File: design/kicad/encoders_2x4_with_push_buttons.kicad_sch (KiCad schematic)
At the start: 0 parts

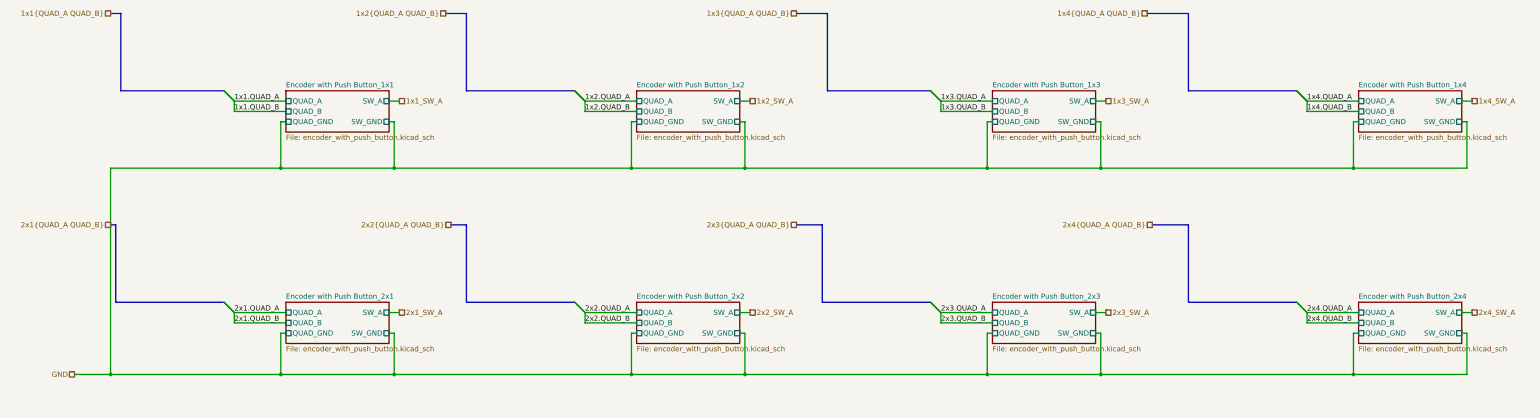
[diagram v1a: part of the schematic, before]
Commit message: Fix hardware pin configuration and rotary encoder parameters
- Updated CS_PIN from 30 to 28 in SystemConstants.hpp to reflect the correct hardware setup for ILI9341.
- Modified rotary encoder parameters in ConfigurationFactory.cpp, changing the first parameter of asRotaryEncoder from 28 to 23 for proper functionality.
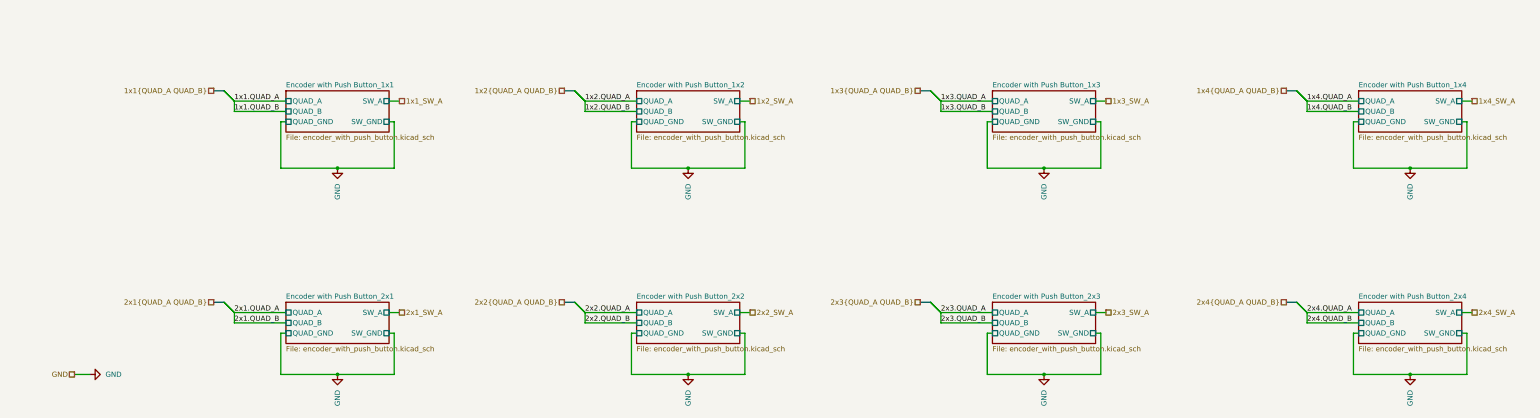
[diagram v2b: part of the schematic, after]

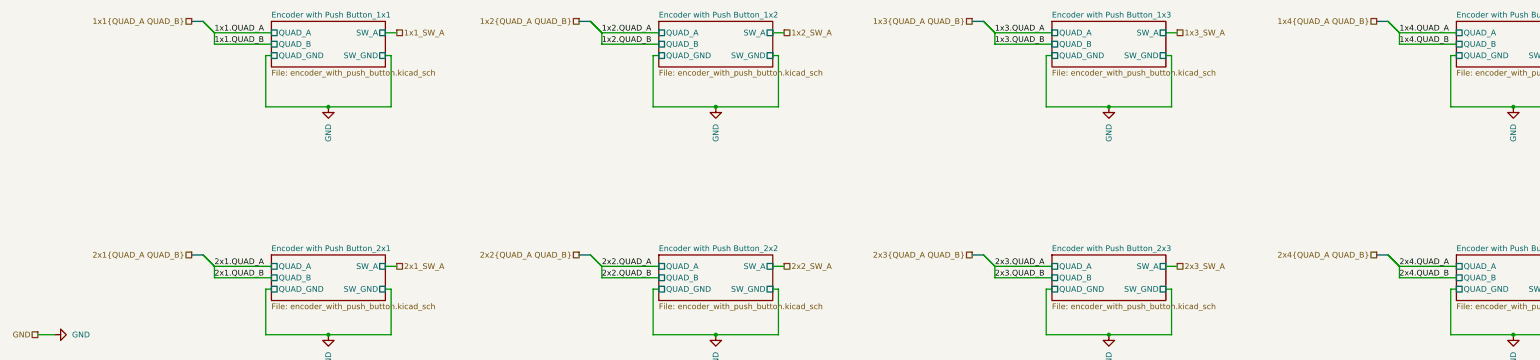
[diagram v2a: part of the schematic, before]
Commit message: Update kicad binary files
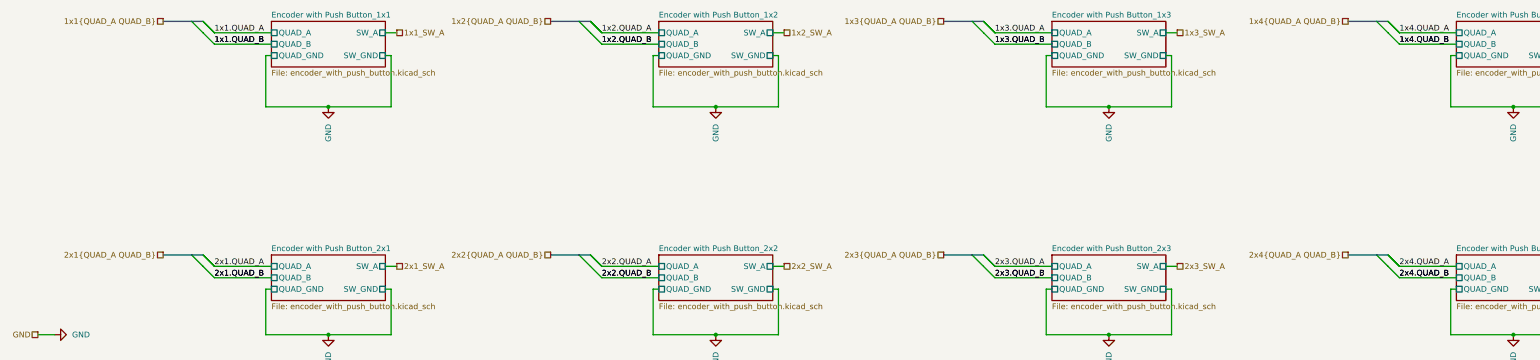
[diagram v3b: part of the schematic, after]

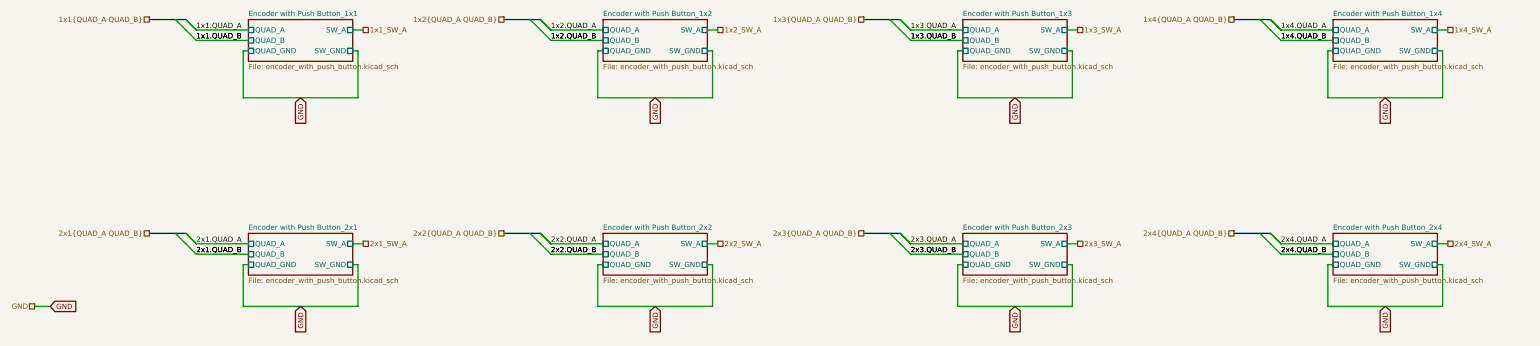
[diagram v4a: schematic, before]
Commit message: Add schematic for MIDI Display MSP2807 with associated components
- Created a new schematic file for the MIDI Display MSP2807.
- Included a unpolarized capacitor (C2) with a value of 100nF.
- Added properties such as reference, value, footprint, and datasheet for the capacitor.
- Integrated the MIDI Display module with detailed pin configurations and properties.
- Defined hierarchical labels for power and data connections (VCC, GND, CS, RST, DC, etc.).
- Ensured all components are marked for BOM inclusion and simulation.
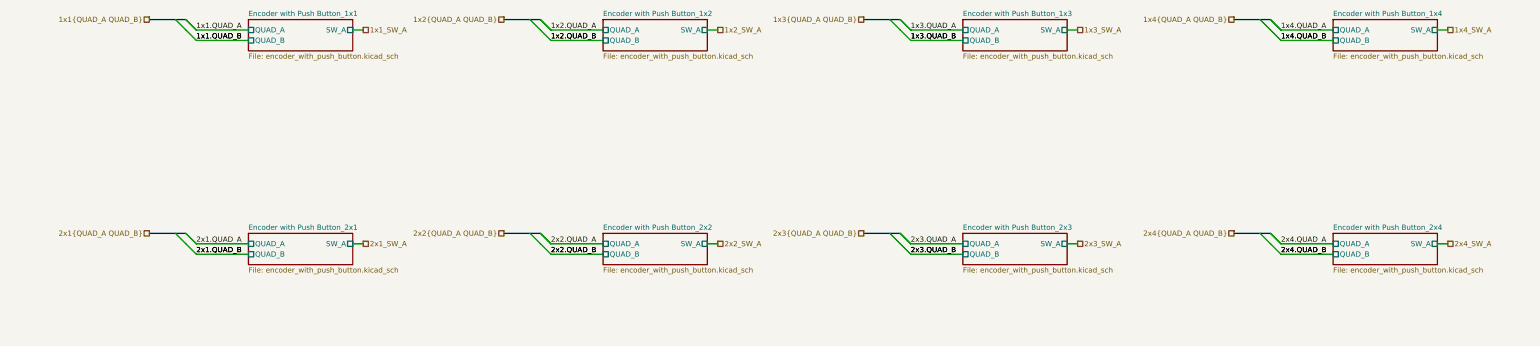
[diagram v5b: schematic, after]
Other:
- sheet Encoder with Push Button_1x1 ports: added none; removed QUAD_GND, SW_GND
- sheet Encoder with Push Button_1x2 ports: added none; removed QUAD_GND, SW_GND
- sheet Encoder with Push Button_1x3 ports: added none; removed QUAD_GND, SW_GND
- sheet Encoder with Push Button_1x4 ports: added none; removed QUAD_GND, SW_GND
- sheet Encoder with Push Button_2x1 ports: added none; removed QUAD_GND, SW_GND
- sheet Encoder with Push Button_2x2 ports: added none; removed QUAD_GND, SW_GND
- sheet Encoder with Push Button_2x3 ports: added none; removed QUAD_GND, SW_GND
- sheet Encoder with Push Button_2x4 ports: added none; removed QUAD_GND, SW_GND

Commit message: Implement code changes to enhance functionality and improve performance
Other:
- sheet Encoder with Push Button_1x1 renamed Encoder_with_Push_Button_1x1
- sheet Encoder with Push Button_1x2 renamed Encoder_with_Push_Button_1x2
- sheet Encoder with Push Button_1x3 renamed Encoder_with_Push_Button_1x3
- sheet Encoder with Push Button_1x4 renamed Encoder_with_Push_Button_1x4
- sheet Encoder with Push Button_2x1 renamed Encoder_with_Push_Button_2x1
- sheet Encoder with Push Button_2x2 renamed Encoder_with_Push_Button_2x2
- sheet Encoder with Push Button_2x3 renamed Encoder_with_Push_Button_2x3
- sheet Encoder with Push Button_2x4 renamed Encoder_with_Push_Button_2x4
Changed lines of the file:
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@@
 			(color 0 0 0 0.0000)
 		)
-		(property "Sheetname" "Encoder with Push Button_1x2"
+		(property "Sheetname" "Encoder_with_Push_Button_1x2"
 			(at 167.64 119.9384 0)
 			(effects
@@
 			(color 0 0 0 0.0000)
 		)
-		(property "Sheetname" "Encoder with Push Button_2x2"
+		(property "Sheetname" "Encoder_with_Push_Button_2x2"
 			(at 167.64 172.0084 0)
 			(effects
@@
 			(color 0 0 0 0.0000)
 		)
-		(property "Sheetname" "Encoder with Push Button_2x3"
+		(property "Sheetname" "Encoder_with_Push_Button_2x3"
 			(at 255.27 172.0084 0)
 			(effects
@@
 			(color 0 0 0 0.0000)
 		)
-		(property "Sheetname" "Encoder with Push Button_1x3"
+		(property "Sheetname" "Encoder_with_Push_Button_1x3"
 			(at 255.27 119.9384 0)
 			(effects
@@
 			(color 0 0 0 0.0000)
 		)
-		(property "Sheetname" "Encoder with Push Button_1x4"
+		(property "Sheetname" "Encoder_with_Push_Button_1x4"
 			(at 345.44 119.9384 0)
 			(effects
@@
 			(color 0 0 0 0.0000)
 		)
-		(property "Sheetname" "Encoder with Push Button_2x1"
+		(property "Sheetname" "Encoder_with_Push_Button_2x1"
 			(at 81.28 172.0084 0)
 			(effects
@@
 			(color 0 0 0 0.0000)
 		)
-		(property "Sheetname" "Encoder with Push Button_1x1"
+		(property "Sheetname" "Encoder_with_Push_Button_1x1"
 			(at 81.28 119.9384 0)
 			(effects
@@
 			(color 0 0 0 0.0000)
 		)
-		(property "Sheetname" "Encoder with Push Button_2x4"
+		(property "Sheetname" "Encoder_with_Push_Button_2x4"
 			(at 345.44 172.0084 0)
 			(effects
